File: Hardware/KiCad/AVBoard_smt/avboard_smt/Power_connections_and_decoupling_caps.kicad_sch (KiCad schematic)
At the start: 44 parts, among them J1 5V

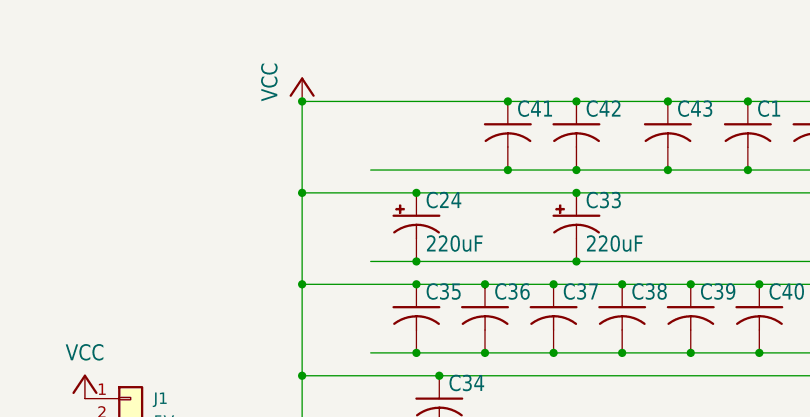
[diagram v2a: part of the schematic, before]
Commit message: Add AV board version with VRAM replaced but not ARAM
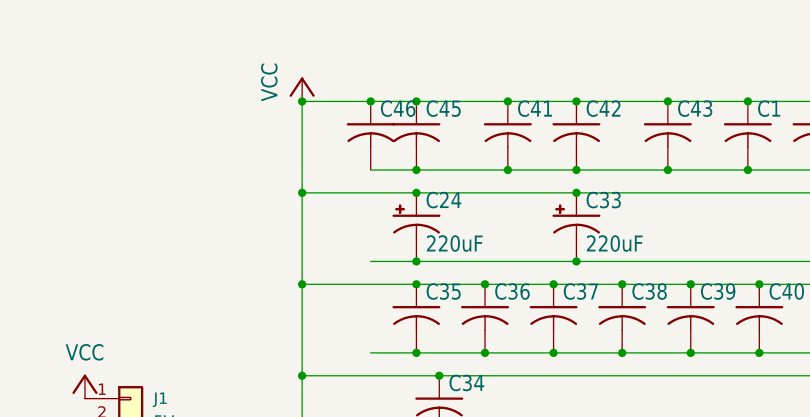
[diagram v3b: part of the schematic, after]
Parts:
- added C45, C46: 0.1uF, Capacitor_SMD:C_0805_2012Metric, symbol signals-eagle-import:C-US025-024X044
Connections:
- net GND: now also C45.2, C46.2
- net VCC: now also C45.1, C46.1
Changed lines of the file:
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@@
 	)
 	(junction
+		(at 121.92 63.5)
+		(diameter 0)
+		(color 0 0 0 0)
+	)
+	(junction
 		(at 182.88 101.6)
 		(diameter 0)
@@
 	)
 	(junction
+		(at 127 63.5)
+		(diameter 0)
+		(color 0 0 0 0)
+	)
+	(junction
 		(at 182.88 91.44)
 		(diameter 0)
@@
 	)
 	(junction
+		(at 127 71.12)
+		(diameter 0)
+		(color 0 0 0 0)
+	)
+	(junction
 		(at 152.4 104.14)
 		(diameter 0)
@@
 	(wire
 		(pts
+			(xy 127 71.12) (xy 137.16 71.12)
+		)
+		(stroke
+			(width 0.1524)
+			(type solid)
+		)
+	)
+	(wire
+		(pts
 			(xy 129.54 101.6) (xy 182.88 101.6)
 		)
@@
 	(wire
 		(pts
-			(xy 121.92 71.12) (xy 137.16 71.12)
+			(xy 121.92 71.12) (xy 127 71.12)
 		)
 		(stroke
@@
 	(wire
 		(pts
+			(xy 121.92 63.5) (xy 127 63.5)
+		)
+		(stroke
+			(width 0.1524)
+			(type solid)
+		)
+	)
+	(wire
+		(pts
 			(xy 137.16 104.14) (xy 144.78 104.14)
 		)
@@
 	(wire
 		(pts
+			(xy 127 63.5) (xy 137.16 63.5)
+		)
+		(stroke
+			(width 0.1524)
+			(type solid)
+		)
+	)
+	(wire
+		(pts
 			(xy 167.64 114.3) (xy 175.26 114.3)
 		)
@@
 	(wire
 		(pts
-			(xy 114.3 63.5) (xy 137.16 63.5)
+			(xy 114.3 63.5) (xy 121.92 63.5)
 		)
 		(stroke
@@
 	(symbol
 		(lib_id "signals-eagle-import:C-US025-024X044")
+		(at 121.92 66.04 0)
+		(unit 1)
+		(exclude_from_sim no)
+		(in_bom yes)
+		(on_board yes)
+		(dnp no)
+		(property "Reference" "C46"
+			(at 122.936 65.405 0)
+			(effects
+				(font
+					(size 1.778 1.5113)
+				)
+				(justify left bottom)
+			)
+		)
+		(property "Value" "0.1uF"
+			(at 122.936 70.231 0)
+			(effects
+				(font
+					(size 1.778 1.5113)
+				)
+				(justify left bottom)
+				(hide yes)
+			)
+		)
+		(property "Footprint" "Capacitor_SMD:C_0805_2012Metric"
+			(at 121.92 66.04 0)
+			(effects
+				(font
+					(size 1.27 1.27)
+				)
+				(hide yes)
+			)
+		)
+		(property "Datasheet" ""
+			(at 121.92 66.04 0)
+			(effects
+				(font
+					(size 1.27 1.27)
+				)
+				(hide yes)
+			)
+		)
+		(property "Description" ""
+			(at 121.92 66.04 0)
+			(effects
+				(font
+					(size 1.27 1.27)
+				)
+			)
+		)
+		(property "MPN" "CC0805KRX7R9BB104"
+			(at 121.92 66.04 0)
+			(effects
+				(font
+					(size 1.27 1.27)
+				)
+				(hide yes)
+			)
+		)
+		(property "Manufacturer_Part_Number" ""
+			(at 121.92 66.04 0)
+			(effects
+				(font
+					(size 1.27 1.27)
+				)
+				(hide yes)
+			)
+		)
+		(pin "1"
+		)
+		(pin "2"
+		)
+		(instances
+			(project "avboard_smt"
+				(path "/ecfc5df0-38b0-48e8-a960-6f082396f7df/bf117f46-6f85-406e-afeb-ad4fbf911792"
+					(reference "C46")
+					(unit 1)
+				)
+			)
+		)
+	)
+	(symbol
+		(lib_id "signals-eagle-import:C-US025-024X044")
 		(at 160.02 106.68 0)
 		(unit 1)
@@
 					(unit 1)
 				)
+			)
+		)
+	)
+	(symbol
+		(lib_id "signals-eagle-import:C-US025-024X044")
+		(at 127 66.04 0)
+		(unit 1)
+		(exclude_from_sim no)
+		(in_bom yes)
+		(on_board yes)
+		(dnp no)
+		(property "Reference" "C45"
+			(at 128.016 65.405 0)
+			(effects
+				(font
+					(size 1.778 1.5113)
+				)
+				(justify left bottom)
+			)
+		)
+		(property "Value" "0.1uF"
+			(at 128.016 70.231 0)
+			(effects
+				(font
+					(size 1.778 1.5113)
+				)
+				(justify left bottom)
+				(hide yes)
+			)
+		)
+		(property "Footprint" "Capacitor_SMD:C_0805_2012Metric"
+			(at 127 66.04 0)
+			(effects
+				(font
+					(size 1.27 1.27)
+				)
+				(hide yes)
+			)
+		)
+		(property "Datasheet" ""
+			(at 127 66.04 0)
+			(effects
+				(font
+					(size 1.27 1.27)
+				)
+				(hide yes)
+			)
+		)
+		(property "Description" ""
+			(at 127 66.04 0)
+			(effects
+				(font
+					(size 1.27 1.27)
+				)
+			)
+		)
+		(property "MPN" "CC0805KRX7R9BB104"
+			(at 127 66.04 0)
+			(effects
+				(font
+					(size 1.27 1.27)
+				)
+				(hide yes)
+			)
+		)
+		(property "Manufacturer_Part_Number" ""
+			(at 127 66.04 0)
+			(effects
+				(font
+					(size 1.27 1.27)
+				)
+				(hide yes)
+			)
+		)
+		(pin "1"
+		)
+		(pin "2"
+		)
+		(instances
+			(project "avboard_smt"
+				(path "/ecfc5df0-38b0-48e8-a960-6f082396f7df/bf117f46-6f85-406e-afeb-ad4fbf911792"
+					(reference "C45")
+					(unit 1)
+				)
